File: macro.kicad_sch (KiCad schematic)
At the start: 62 parts, among them J1 Conn_01x01_Male, J2 Conn_01x01_Male, J3 Conn_01x01_Male, Q1 BSS138, SW1 RotaryEncoder_Switch, SW2 SW_Push, U1 AP2112K-3.3, U2 W25Q128JVPIQ, U3 RP2040, Y1 12MHz

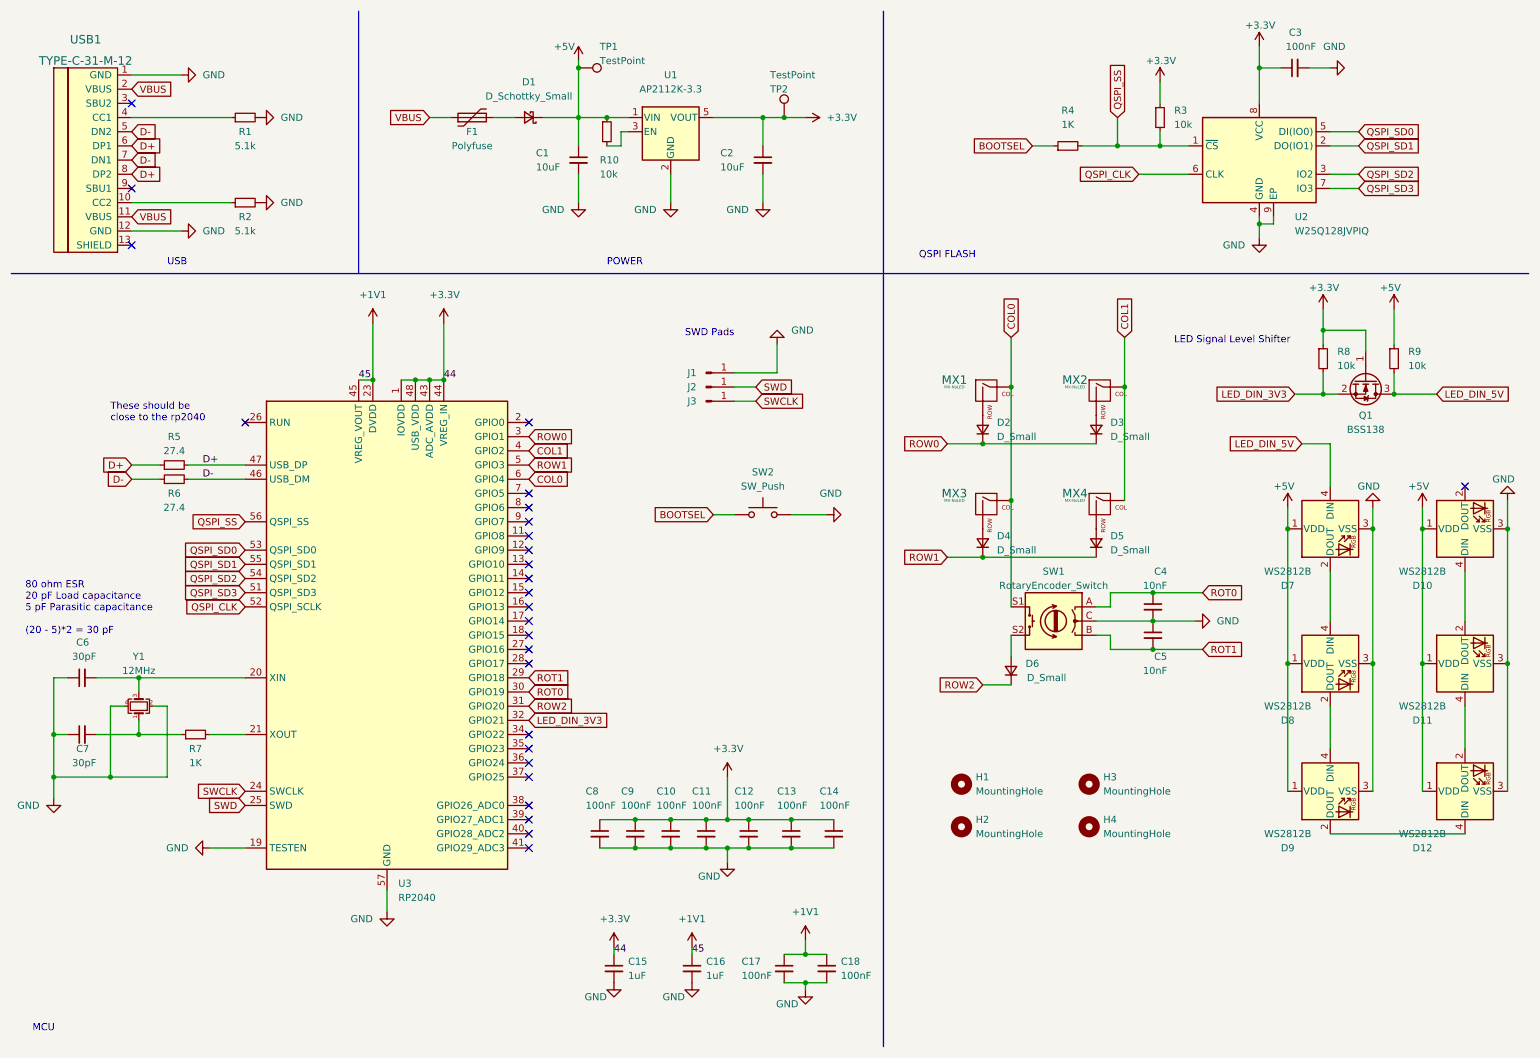
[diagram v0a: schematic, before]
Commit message: Add tooling holes and logo
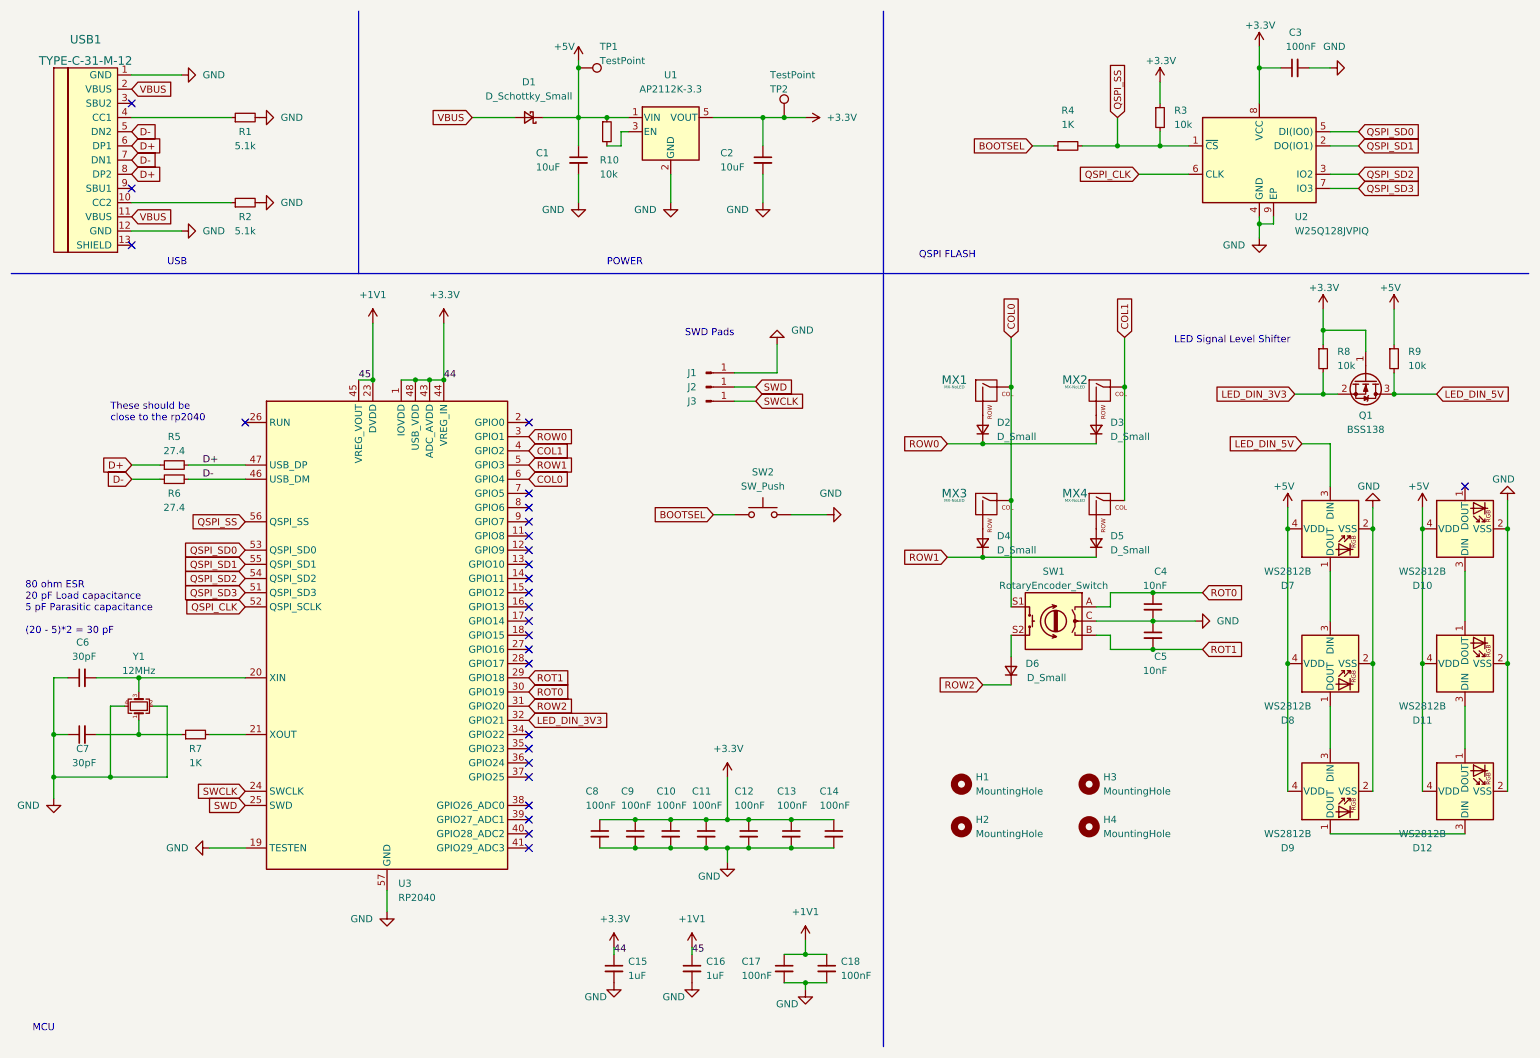
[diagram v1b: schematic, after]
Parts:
- removed F1: Polyfuse, Fuse:Fuse_0402_1005Metric, symbol Device:Polyfuse
- D10, D11, D12, D7, D8, D9: symbol LED:WS2812B -> LED:WS2812B_JLC
- J1, J2, J3, MX1, MX2, MX3, MX4, TP1, TP2: now left out of the parts list
- SW2: footprint Button_Switch_SMD:SW_Push_1P1T_NO_CK_KMR2 -> KMR221GLFS:SW_KMR221GLFS
- USB1: footprint Type-C:HRO-TYPE-C-31-M-12-Assembly -> TYPE-C-31-M-12:HRO_TYPE-C-31-M-12
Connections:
- net +5V: now also D10.4 (VDD), D11.4 (VDD), D12.4 (VDD), D7.4 (VDD), D8.4 (VDD), D9.4 (VDD); no longer D10.1 (VDD), D11.1 (VDD), D12.1 (VDD), D7.1 (VDD), D8.1 (VDD), D9.1 (VDD)
- net GND: now also D10.2 (VSS), D11.2 (VSS), D12.2 (VSS), D7.2 (VSS), D8.2 (VSS), D9.2 (VSS); no longer D10.3 (VSS), D11.3 (VSS), D12.3 (VSS), D7.3 (VSS), D8.3 (VSS), D9.3 (VSS)
- net LED_DIN_5V: now also D7.3 (DIN); no longer D7.4 (DIN)
- net VBUS: now also D1.2 (A)
- new net: D7.1 (DOUT), D8.3 (DIN)
- new net: D11.3 (DIN), D12.1 (DOUT)
- new net: D12.3 (DIN), D9.1 (DOUT)
- new net: D8.1 (DOUT), D9.3 (DIN)
- new net: D10.3 (DIN), D11.1 (DOUT)
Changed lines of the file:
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@@
-    (stroke (width 0) (type default) (color 0 0 0 0))
-  )
-  (wire (pts (xy 99.06 31.75) (xy 102.87 31.75))
     (stroke (width 0) (type default) (color 0 0 0 0))
   )
@@
     (stroke (width 0) (type default) (color 0 0 0 0))
   )
-  (wire (pts (xy 87.63 31.75) (xy 91.44 31.75))
+  (wire (pts (xy 95.25 31.75) (xy 102.87 31.75))
     (stroke (width 0) (type default) (color 0 0 0 0))
   )
@@
     )
   )
-  (global_label "VBUS" (shape input) (at 87.63 31.75 180) (fields_autoplaced)
+  (global_label "VBUS" (shape input) (at 95.25 31.75 180) (fields_autoplaced)
     (effects (font (size 1.27 1.27)) (justify right))
-    (property "Intersheet References" "${INTERSHEET_REFS}" (id 0) (at 80.3183 31.8294 0)
+    (property "Intersheet References" "${INTERSHEET_REFS}" (id 0) (at 87.9383 31.8294 0)
       (effects (font (size 1.27 1.27)) (justify right) hide)
     )
@@
     )
   )
-  (symbol (lib_id "LED:WS2812B") (at 248.92 105.41 90) (mirror x) (unit 1)
+  (symbol (lib_id "LED:WS2812B_JLC") (at 248.92 105.41 90) (mirror x) (unit 1)
     (in_bom yes) (on_board yes)
     (property "Reference" "D7" (id 0) (at 241.3 115.57 90))
@@
   )
   (symbol (lib_id "MX_Alps_Hybrid:MX-NoLED") (at 187.96 101.6 0) (unit 1)
-    (in_bom yes) (on_board yes)
+    (in_bom no) (on_board yes)
     (property "Reference" "MX3" (id 0) (at 181.61 99.06 0)
       (effects (font (size 1.524 1.524)))
@@
     (pin "2")
   )
-  (symbol (lib_id "LED:WS2812B") (at 273.05 152.4 90) (unit 1)
+  (symbol (lib_id "LED:WS2812B_JLC") (at 273.05 152.4 90) (unit 1)
     (in_bom yes) (on_board yes)
     (property "Reference" "D12" (id 0) (at 265.43 162.56 90))
@@
     (pin "1")
   )
-  (symbol (lib_id "Device:Polyfuse") (at 95.25 31.75 90) (unit 1)
-    (in_bom yes) (on_board yes)
-    (property "Reference" "F1" (id 0) (at 95.25 34.29 90))
-    (property "Value" "Polyfuse" (id 1) (at 95.25 36.83 90))
-    (property "Footprint" "Fuse:Fuse_0402_1005Metric" (id 2) (at 100.33 30.48 0)
-      (effects (font (size 1.27 1.27)) (justify left) hide)
-    )
-    (property "Datasheet" "~" (id 3) (at 95.25 31.75 0)
-      (effects (font (size 1.27 1.27)) hide)
-    )
-    (pin "1")
-    (pin "2")
-  )
   (symbol (lib_id "power:+5V") (at 241.3 101.6 0) (mirror y) (unit 1)
     (in_bom yes) (on_board yes)
@@
   )
   (symbol (lib_id "Connector:TestPoint") (at 151.13 31.75 0) (unit 1)
-    (in_bom yes) (on_board yes)
+    (in_bom no) (on_board yes)
     (property "Reference" "TP2" (id 0) (at 148.59 26.67 0)
       (effects (font (size 1.27 1.27)) (justify left))
@@
     (pin "1")
   )
-  (symbol (lib_id "LED:WS2812B") (at 248.92 152.4 90) (mirror x) (unit 1)
+  (symbol (lib_id "LED:WS2812B_JLC") (at 248.92 152.4 90) (mirror x) (unit 1)
     (in_bom yes) (on_board yes)
     (property "Reference" "D9" (id 0) (at 241.3 162.56 90))
@@
   )
   (symbol (lib_id "Connector:Conn_01x01_Male") (at 137.16 80.01 0) (unit 1)
-    (in_bom yes) (on_board yes)
+    (in_bom no) (on_board yes)
     (property "Reference" "J2" (id 0) (at 134.62 80.01 0))
     (property "Value" "Conn_01x01_Male" (id 1) (at 137.795 77.47 0)
@@
       (effects (font (size 1.524 1.524)))
     )
-    (property "Footprint" "Type-C:HRO-TYPE-C-31-M-12-Assembly" (id 2) (at 31.75 38.1 0)
+    (property "Footprint" "TYPE-C-31-M-12:HRO_TYPE-C-31-M-12" (id 2) (at 31.75 38.1 0)
       (effects (font (size 1.524 1.524)) hide)
     )
@@
     (pin "1")
   )
-  (symbol (lib_id "LED:WS2812B") (at 273.05 105.41 90) (unit 1)
+  (symbol (lib_id "LED:WS2812B_JLC") (at 273.05 105.41 90) (unit 1)
     (in_bom yes) (on_board yes)
     (property "Reference" "D10" (id 0) (at 265.43 115.57 90))
@@
     (property "Reference" "SW2" (id 0) (at 147.32 95.25 0))
     (property "Value" "SW_Push" (id 1) (at 147.32 97.79 0))
-    (property "Footprint" "Button_Switch_SMD:SW_Push_1P1T_NO_CK_KMR2" (id 2) (at 147.32 97.79 0)
+    (property "Footprint" "KMR221GLFS:SW_KMR221GLFS" (id 2) (at 147.32 97.79 0)
       (effects (font (size 1.27 1.27)) hide)
     )
@@
     (pin "2")
   )
-  (symbol (lib_id "LED:WS2812B") (at 248.92 129.54 90) (mirror x) (unit 1)
+  (symbol (lib_id "LED:WS2812B_JLC") (at 248.92 129.54 90) (mirror x) (unit 1)
     (in_bom yes) (on_board yes)
     (property "Reference" "D8" (id 0) (at 241.3 139.7 90))
@@
   )
   (symbol (lib_id "MX_Alps_Hybrid:MX-NoLED") (at 187.96 81.28 0) (unit 1)
-    (in_bom yes) (on_board yes)
+    (in_bom no) (on_board yes)
     (property "Reference" "MX1" (id 0) (at 181.61 78.74 0)
       (effects (font (size 1.524 1.524)))
@@
   )
   (symbol (lib_id "Connector:Conn_01x01_Male") (at 137.16 82.55 0) (unit 1)
-    (in_bom yes) (on_board yes)
+    (in_bom no) (on_board yes)
     (property "Reference" "J3" (id 0) (at 134.62 82.55 0))
     (property "Value" "Conn_01x01_Male" (id 1) (at 137.795 80.01 0)
@@
     (pin "1")
   )
-  (symbol (lib_id "LED:WS2812B") (at 273.05 129.54 90) (unit 1)
+  (symbol (lib_id "LED:WS2812B_JLC") (at 273.05 129.54 90) (unit 1)
     (in_bom yes) (on_board yes)
     (property "Reference" "D11" (id 0) (at 265.43 139.7 90))
@@
   )
   (symbol (lib_id "Connector:TestPoint") (at 114.3 22.86 270) (unit 1)
-    (in_bom yes) (on_board yes)
+    (in_bom no) (on_board yes)
     (property "Reference" "TP1" (id 0) (at 118.11 19.05 90)
       (effects (font (size 1.27 1.27)) (justify left))
@@
   )
   (symbol (lib_id "Connector:Conn_01x01_Male") (at 137.16 77.47 0) (unit 1)
-    (in_bom yes) (on_board yes)
+    (in_bom no) (on_board yes)
     (property "Reference" "J1" (id 0) (at 134.62 77.47 0))
     (property "Value" "Conn_01x01_Male" (id 1) (at 137.795 74.93 0)
@@
   )
   (symbol (lib_id "MX_Alps_Hybrid:MX-NoLED") (at 208.28 101.6 0) (unit 1)
-    (in_bom yes) (on_board yes)
+    (in_bom no) (on_board yes)
     (property "Reference" "MX4" (id 0) (at 203.2 99.06 0)
       (effects (font (size 1.524 1.524)))
@@
   )
   (symbol (lib_id "MX_Alps_Hybrid:MX-NoLED") (at 208.28 81.28 0) (unit 1)
-    (in_bom yes) (on_board yes)
+    (in_bom no) (on_board yes)
     (property "Reference" "MX2" (id 0) (at 203.2 78.74 0)
       (effects (font (size 1.524 1.524)))
@@
       (reference "D12") (unit 1) (value "WS2812B") (footprint "LED_SMD:LED_WS2812B-2020_PLCC4_2.0x2.0mm")
     )
-    (path "/29a50d2e-63d6-4df3-a6e1-8bb59443e80d"
-      (reference "F1") (unit 1) (value "Polyfuse") (footprint "Fuse:Fuse_0402_1005Metric")
-    )
     (path "/1d70f394-b2a7-47ea-9c80-cc301d38760c"
       (reference "H1") (unit 1) (value "MountingHole") (footprint "MountingHole:MountingHole_2.2mm_M2")
@@
     )
     (path "/7a8be5f3-2d02-4f51-8b71-3acb1026b12b"
-      (reference "SW2") (unit 1) (value "SW_Push") (footprint "Button_Switch_SMD:SW_Push_1P1T_NO_CK_KMR2")
+      (reference "SW2") (unit 1) (value "SW_Push") (footprint "KMR221GLFS:SW_KMR221GLFS")
     )
     (path "/b7bb6635-cf66-4553-8332-a379ea2e3c29"
@@
     )
     (path "/52739d50-306c-4509-aab9-db79191c5ef8"
-      (reference "USB1") (unit 1) (value "TYPE-C-31-M-12") (footprint "Type-C:HRO-TYPE-C-31-M-12-Assembly")
+      (reference "USB1") (unit 1) (value "TYPE-C-31-M-12") (footprint "TYPE-C-31-M-12:HRO_TYPE-C-31-M-12")
     )
     (path "/d0af3636-4ad8-40cf-82ca-03a2b9618944"

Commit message: V0.1 Version
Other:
- company: (none) -> Nick Yu
- title: (none) -> duckboard
- moved on the sheet: R3
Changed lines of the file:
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@@
 (kicad_sch (version 20211123) (generator eeschema)
   (paper "A4")
+  (title_block
+    (title "duckboard")
+    (date "2023-01-07")
+    (rev "v0.1")
+    (company "Nick Yu")
+  )
   (junction (at 280.67 105.41) (diameter 0) (color 0 0 0 0)
   )
@@
   (junction (at 124.46 157.48) (diameter 0) (color 0 0 0 0)
   )
-  (junction (at 210.82 36.83) (diameter 0) (color 0 0 0 0)
+  (junction (at 219.71 36.83) (diameter 0) (color 0 0 0 0)
   )
   (junction (at 140.97 162.56) (diameter 0) (color 0 0 0 0)
@@
   (junction (at 87.63 78.74) (diameter 0) (color 0 0 0 0)
   )
-  (junction (at 218.44 36.83) (diameter 0) (color 0 0 0 0)
+  (junction (at 209.55 36.83) (diameter 0) (color 0 0 0 0)
   )
   (junction (at 256.54 105.41) (diameter 0) (color 0 0 0 0)
@@
     (stroke (width 0) (type default) (color 0 0 0 0))
   )
-  (wire (pts (xy 218.44 36.83) (xy 218.44 34.29))
+  (wire (pts (xy 209.55 36.83) (xy 209.55 34.29))
     (stroke (width 0) (type default) (color 0 0 0 0))
   )
@@
     (stroke (width 0) (type default) (color 0 0 0 0))
   )
-  (wire (pts (xy 204.47 36.83) (xy 210.82 36.83))
-    (stroke (width 0) (type default) (color 0 0 0 0))
-  )
-  (wire (pts (xy 210.82 31.75) (xy 210.82 36.83))
+  (wire (pts (xy 204.47 36.83) (xy 209.55 36.83))
+    (stroke (width 0) (type default) (color 0 0 0 0))
+  )
+  (wire (pts (xy 219.71 31.75) (xy 219.71 36.83))
     (stroke (width 0) (type default) (color 0 0 0 0))
   )
@@
     (stroke (width 0) (type default) (color 0 0 0 0))
   )
-  (wire (pts (xy 223.52 36.83) (xy 218.44 36.83))
-    (stroke (width 0) (type default) (color 0 0 0 0))
-  )
   (wire (pts (xy 236.22 50.8) (xy 236.22 53.34))
     (stroke (width 0) (type default) (color 0 0 0 0))
@@
     (stroke (width 0) (type default) (color 0 0 0 0))
   )
-  (wire (pts (xy 210.82 36.83) (xy 218.44 36.83))
+  (wire (pts (xy 219.71 36.83) (xy 209.55 36.83))
     (stroke (width 0) (type default) (color 0 0 0 0))
   )
@@
     (stroke (width 0) (type default) (color 0 0 0 0))
   )
+  (wire (pts (xy 219.71 36.83) (xy 223.52 36.83))
+    (stroke (width 0) (type default) (color 0 0 0 0))
+  )
   (wire (pts (xy 186.69 133.35) (xy 191.77 133.35))
     (stroke (width 0) (type default) (color 0 0 0 0))
@@
     (stroke (width 0) (type default) (color 0 0 0 0))
   )
-  (wire (pts (xy 218.44 25.4) (xy 218.44 29.21))
+  (wire (pts (xy 209.55 25.4) (xy 209.55 29.21))
     (stroke (width 0) (type default) (color 0 0 0 0))
   )
@@
     )
   )
-  (global_label "QSPI_SS" (shape input) (at 210.82 31.75 90) (fields_autoplaced)
-    (effects (font (size 1.27 1.27)) (justify left))
-    (property "Intersheet References" "${INTERSHEET_REFS}" (id 0) (at 210.7406 21.5355 90)
+  (global_label "QSPI_SS" (shape input) (at 219.71 31.75 90) (fields_autoplaced)
+    (effects (font (size 1.27 1.27)) (justify left))
+    (property "Intersheet References" "${INTERSHEET_REFS}" (id 0) (at 219.6306 21.5355 90)
       (effects (font (size 1.27 1.27)) (justify left) hide)
     )
@@
     (pin "2")
   )
-  (symbol (lib_id "power:+3.3V") (at 218.44 25.4 0) (unit 1)
-    (in_bom yes) (on_board yes)
-    (property "Reference" "#PWR011" (id 0) (at 218.44 29.21 0)
-      (effects (font (size 1.27 1.27)) hide)
-    )
-    (property "Value" "+3.3V" (id 1) (at 215.9 21.59 0)
-      (effects (font (size 1.27 1.27)) (justify left))
-    )
-    (property "Footprint" "" (id 2) (at 218.44 25.4 0)
-      (effects (font (size 1.27 1.27)) hide)
-    )
-    (property "Datasheet" "" (id 3) (at 218.44 25.4 0)
+  (symbol (lib_id "power:+3.3V") (at 209.55 25.4 0) (unit 1)
+    (in_bom yes) (on_board yes)
+    (property "Reference" "#PWR011" (id 0) (at 209.55 29.21 0)
+      (effects (font (size 1.27 1.27)) hide)
+    )
+    (property "Value" "+3.3V" (id 1) (at 207.01 21.59 0)
+      (effects (font (size 1.27 1.27)) (justify left))
+    )
+    (property "Footprint" "" (id 2) (at 209.55 25.4 0)
+      (effects (font (size 1.27 1.27)) hide)
+    )
+    (property "Datasheet" "" (id 3) (at 209.55 25.4 0)
       (effects (font (size 1.27 1.27)) hide)
     )
@@
     (pin "2")
   )
-  (symbol (lib_id "Device:R_Small") (at 218.44 31.75 0) (unit 1)
+  (symbol (lib_id "Device:R_Small") (at 209.55 31.75 0) (unit 1)
     (in_bom yes) (on_board yes) (fields_autoplaced)
-    (property "Reference" "R3" (id 0) (at 220.98 30.4799 0)
-      (effects (font (size 1.27 1.27)) (justify left))
-    )
-    (property "Value" "10k" (id 1) (at 220.98 33.0199 0)
-      (effects (font (size 1.27 1.27)) (justify left))
-    )
-    (property "Footprint" "Resistor_SMD:R_0402_1005Metric" (id 2) (at 218.44 31.75 0)
-      (effects (font (size 1.27 1.27)) hide)
-    )
-    (property "Datasheet" "~" (id 3) (at 218.44 31.75 0)
-      (effects (font (size 1.27 1.27)) hide)
-    )
+    (property "Reference" "R3" (id 0) (at 212.09 30.4799 0)
+      (effects (font (size 1.27 1.27)) (justify left))
+    )
+    (property "Value" "10k" (id 1) (at 212.09 33.0199 0)
+      (effects (font (size 1.27 1.27)) (justify left))
+    )
+    (property "Footprint" "Resistor_SMD:R_0402_1005Metric" (id 2) (at 209.55 31.75 0)
+      (effects (font (size 1.27 1.27)) hide)
+    )
+    (property "Datasheet" "~" (id 3) (at 209.55 31.75 0)
+      (effects (font (size 1.27 1.27)) hide)
+    )
